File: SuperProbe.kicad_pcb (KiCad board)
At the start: 2 copper layers, 100 x 45 mm, 66 parts, among them J1 Conn_01x01, J10 Conn_01x01, J11 Conn_01x01, J12 Conn_01x01, J13 Conn_01x01, J14 Conn_01x01, J15 Conn_01x01, J16 Conn_01x01, J17 Conn_01x02, J2 Conn_01x01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

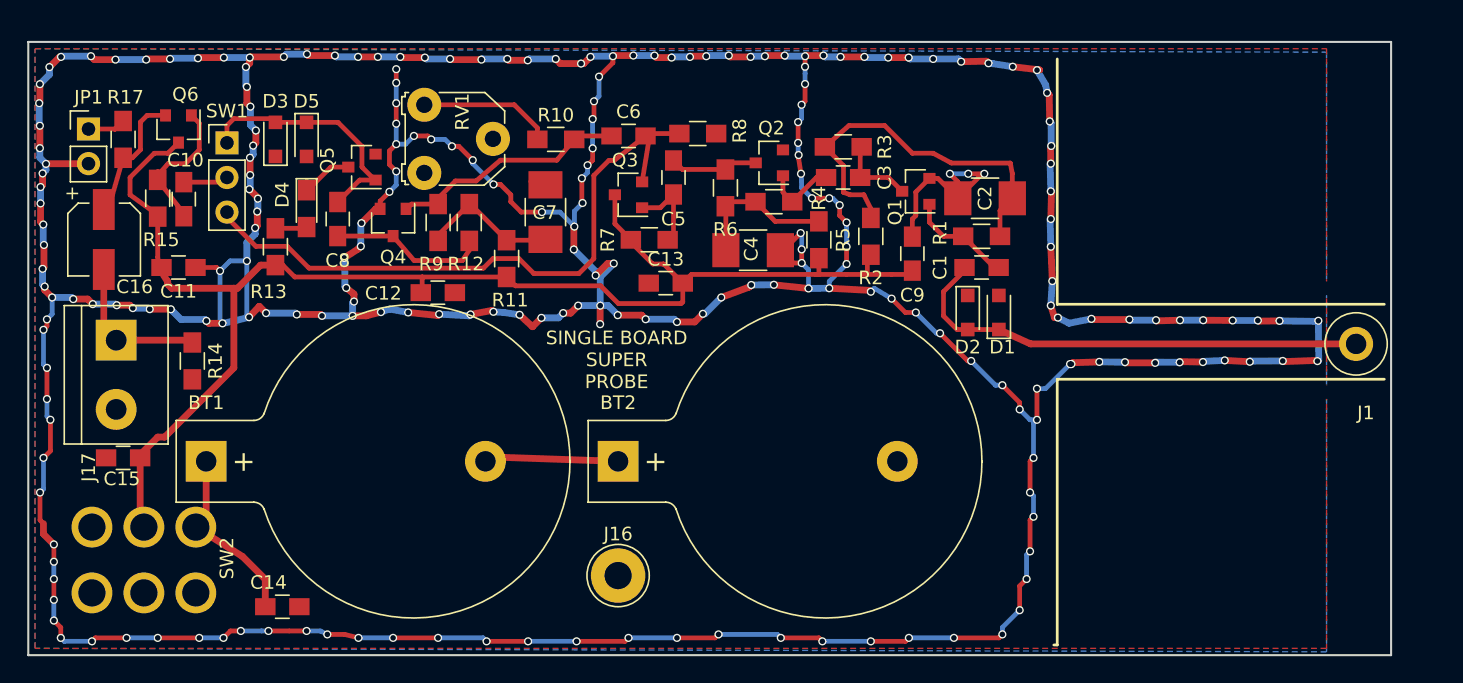
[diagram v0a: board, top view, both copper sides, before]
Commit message: Uses 9 volt battery and board shrink
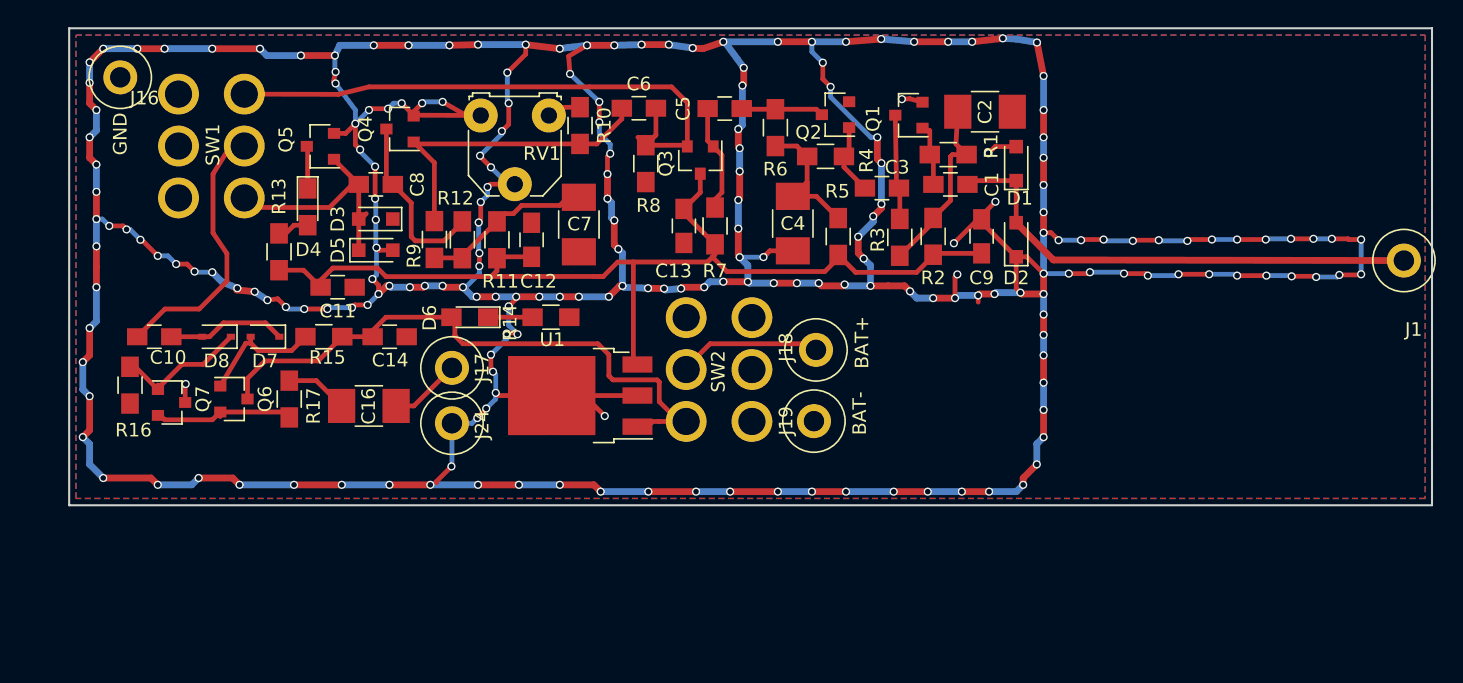
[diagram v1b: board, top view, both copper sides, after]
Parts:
- removed BT1, BT2: Battery_Cell, Battery_Holders:Keystone_103_1x20mm-CoinCell
- removed C15: 100 nF, Capacitors_SMD:C_0805_HandSoldering
- removed JP1: Jumper_NO_Small, Pin_Headers:Pin_Header_Straight_1x02_Pitch2.54mm
- added D6: LED, LEDs:LED_0805_HandSoldering, F.Cu at (70.4, 102.2)
- added D7: 1N4148WS, Diodes_SMD:D_SOD-323, F.Cu at (55.4, 103.6)
- added D8: 1N4148WS, Diodes_SMD:D_SOD-323, F.Cu at (51.8, 103.6)
- added J18: Conn_01x01, Connectors:1pin, F.Cu at (95.8, 104.6)
- added J19: Conn_01x01, Connectors:1pin, F.Cu at (95.7, 109.8)
- added J20: Conn_01x01, SuperProbe:BigSlot, F.Cu at (108.2, 110.0)
- added J21: Conn_01x01, SuperProbe:BigSlot, F.Cu at (102.0, 110.0)
- added J22: Conn_01x01, SuperProbe:BigSlot, F.Cu at (108.2, 84.3)
- added J23: Conn_01x01, SuperProbe:BigSlot, F.Cu at (102.1, 84.4)
- added J24: Conn_01x01, Connectors:1pin, F.Cu at (69.1, 110.0)
- added Q7: MMBT3906, TO_SOT_Packages_SMD:SOT-23, F.Cu at (48.5, 108.5)
- added R16: 10k, Resistors_SMD:R_0805_HandSoldering, F.Cu at (45.5, 107.2)
- added U1: LM78M05_TO252, TO_SOT_Packages_SMD:TO-252-3_TabPin2, F.Cu at (78.5, 108.0)
- C14: value 100 nF -> 1 uF
- C16: value 100 uF -> 22 uF; footprint Capacitors_SMD:CP_Elec_5x5.3 -> Capacitors_SMD:C_1210_HandSoldering
- J17: value Conn_01x02 -> Conn_01x01; footprint Connectors_Terminal_Blocks:TerminalBlock_bornier-2_P5.08mm -> Connectors:1pin
- R14: value 10k -> 1k
- R15: value 3M3 -> 10k
- R17: value 10k -> 100R
- SW1: footprint Pin_Headers:Pin_Header_Straight_1x03_Pitch2.54mm -> SuperProbe:DPDTsmallswitch
- moved J16 51.7 mm to (44.8, 84.6)
- moved SW2 41.5 mm to (91.1, 109.8), turned to 90 degrees
- moved J15 39.9 mm to (114.6, 82.8)
- moved J14 29.7 mm to (114.6, 87.1)
- moved J8 28.2 mm to (114.6, 113.8)
- moved R14 26.5 mm to (76.3, 102.2), turned to 0 degrees
- moved J17 24.7 mm to (69.1, 105.9), turned to 0 degrees
- moved C16 23.0 mm to (63.0, 108.7), turned to 180 degrees
- moved R17 22.6 mm to (57.1, 108.2), turned to 270 degrees
- moved C14 21.3 mm to (64.5, 103.6)
- moved Q6 20.2 mm to (53.1, 108.2), turned to 0 degrees
- moved J9 17.8 mm to (114.6, 93.0)
- moved J7 17.8 mm to (114.6, 109.2)
- moved R15 15.9 mm to (59.7, 103.6), turned to 180 degrees
- moved J13 13.4 mm to (136.9, 94.5)
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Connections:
- C14 pad 2: Net-(BT1-Pad1) -> +9V
- J17 pad 1: Net-(C16-Pad2) -> Net-(C16-Pad1)
- Q6 pad 1: Net-(C10-Pad1) -> Net-(D7-Pad2)
- Q6 pad 2: Net-(C16-Pad1) -> Net-(Q6-Pad2)
- Q6 pad 3: +5V -> +9V
- R14 pad 1: Net-(C16-Pad2) -> Net-(D6-Pad1)
- R15 pad 1: +5V -> +9V
- R15 pad 2: Net-(C10-Pad1) -> Net-(D7-Pad2)
- R17 pad 1: Net-(C16-Pad1) -> Net-(C16-Pad2)
- R17 pad 2: Net-(JP1-Pad1) -> Net-(Q6-Pad2)
- SW2 pad 1: Net-(BT1-Pad1) -> (no net)
- SW2 pad 2: +5V -> (no net)
- SW2 pad 4: (no net) -> +9V
- SW2 pad 5: (no net) -> Net-(J18-Pad1)
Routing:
- net +9V: track 0.00 -> 46.2 mm
- net +5V: track 108.0 -> 76.1 mm
- net GND: track 490.7 -> 514.7 mm, vias 233 -> 216
- net Net-(C10-Pad2): track 3.31 -> 21.6 mm
- net Net-(BT1-Pad1): track 15.3 -> 0.00 mm
- net Net-(C2-Pad1): track 28.2 -> 13.5 mm
- net Net-(Q6-Pad2): track 0.00 -> 10.6 mm
- net Net-(J18-Pad1): track 0.00 -> 10.6 mm
- net Net-(D8-Pad1): track 0.00 -> 10.1 mm
- net Net-(BT1-Pad2): track 9.88 -> 0.00 mm
- net Net-(C16-Pad2): track 14.3 -> 4.61 mm
- net Net-(D7-Pad2): track 0.00 -> 9.16 mm
- net Net-(R10-Pad2): track 10.1 -> 2.53 mm
- net Net-(C6-Pad1): track 17.7 -> 23.3 mm
- net Net-(C16-Pad1): track 9.79 -> 5.25 mm
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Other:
- board size 100 x 45 mm -> 100 x 35 mm
- board text added: "BAT+"
- board text added: "BAT-"
- board text added: "GND"

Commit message: Cleaned up the board slightly
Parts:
- C10: value 10 nF -> 100 nF
- C16, C2, C4, C7: footprint Capacitors_SMD:C_1210_HandSoldering -> Capacitors_SMD:C_0805_HandSoldering
- C8: value 360 pF -> 330 pF
- J1, J16, J17, J18, J19, J24: footprint Connectors:1pin -> SuperProbe:PadHole
- Q6: value MMBT3904 -> S8050
- Q7: value MMBT3906 -> S8550
- R1, R4, R7, R9: value 3M3 -> 2M2
- R17: value 100R -> 47R
- moved J8 1.01 mm to (114.5, 112.8)
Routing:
- net GND: track 514.7 -> 512.7 mm
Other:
- board size 100 x 35 mm -> 100 x 34 mm
- board text added: "SPK+"
- board text added: "SPK-"

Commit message: Eliminated unneeded diode
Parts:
- removed D3: LRB751V, Diodes_SMD:D_SOD-323_HandSoldering
- Q6: value S8050 -> SS8050
- Q7: value S8550 -> SS8550
- moved D5 2.29 mm to (63.5, 95.0)
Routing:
- net Net-(C8-Pad1): track 17.6 -> 14.6 mm
- net GND: track 512.7 -> 513.0 mm, vias 216 -> 215
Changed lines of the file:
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@@
 (kicad_pcb (version 4) (host pcbnew 4.0.7)
   (general
-    (links 95)
+    (links 93)
     (no_connects 0)
     (area 40.002381 78.05638 143.68562 117.528699)
     (thickness 1.6)
     (drawings 10)
-    (tracks 822)
+    (tracks 819)
     (zones 0)
-    (modules 75)
+    (modules 74)
     (nets 29)
   )
@@
     )
   )
-  (module Diodes_SMD:D_SOD-323_HandSoldering (layer F.Cu)
-    (at 63.5 94.996 180)
-    (descr SOD-323)
-    (tags SOD-323)
-    (attr smd)
-    (fp_text reference D3 (at 2.794 0 270) (layer F.SilkS)
-      (effects (font (size 1 1) (thickness 0.15)))
-    )
-    (fp_text value LRB751V (at 0.1 1.9 180) (layer F.Fab)
-      (effects (font (size 1 1) (thickness 0.15)))
-    )
-    (fp_text user %R (at 0 -1.85 180) (layer F.Fab)
-      (effects (font (size 1 1) (thickness 0.15)))
-    )
-    (fp_line (start -1.9 -0.85) (end -1.9 0.85) (layer F.SilkS) (width 0.12))
-    (fp_line (start 0.2 0) (end 0.45 0) (layer F.Fab) (width 0.1))
-    (fp_line (start 0.2 0.35) (end -0.3 0) (layer F.Fab) (width 0.1))
-    (fp_line (start 0.2 -0.35) (end 0.2 0.35) (layer F.Fab) (width 0.1))
-    (fp_line (start -0.3 0) (end 0.2 -0.35) (layer F.Fab) (width 0.1))
-    (fp_line (start -0.3 0) (end -0.5 0) (layer F.Fab) (width 0.1))
-    (fp_line (start -0.3 -0.35) (end -0.3 0.35) (layer F.Fab) (width 0.1))
-    (fp_line (start -0.9 0.7) (end -0.9 -0.7) (layer F.Fab) (width 0.1))
-    (fp_line (start 0.9 0.7) (end -0.9 0.7) (layer F.Fab) (width 0.1))
-    (fp_line (start 0.9 -0.7) (end 0.9 0.7) (layer F.Fab) (width 0.1))
-    (fp_line (start -0.9 -0.7) (end 0.9 -0.7) (layer F.Fab) (width 0.1))
-    (fp_line (start -2 -0.95) (end 2 -0.95) (layer F.CrtYd) (width 0.05))
-    (fp_line (start 2 -0.95) (end 2 0.95) (layer F.CrtYd) (width 0.05))
-    (fp_line (start -2 0.95) (end 2 0.95) (layer F.CrtYd) (width 0.05))
-    (fp_line (start -2 -0.95) (end -2 0.95) (layer F.CrtYd) (width 0.05))
-    (fp_line (start -1.9 0.85) (end 1.25 0.85) (layer F.SilkS) (width 0.12))
-    (fp_line (start -1.9 -0.85) (end 1.25 -0.85) (layer F.SilkS) (width 0.12))
-    (pad 1 smd rect (at -1.25 0 180) (size 1 1) (layers F.Cu F.Paste F.Mask)
-      (net 1 GND))
-    (pad 2 smd rect (at 1.25 0 180) (size 1 1) (layers F.Cu F.Paste F.Mask)
-      (net 13 "Net-(C8-Pad1)"))
-    (model ${KISYS3DMOD}/Diodes_SMD.3dshapes/D_SOD-323.wrl
-      (at (xyz 0 0 0))
-      (scale (xyz 1 1 1))
-      (rotate (xyz 0 0 0))
-    )
-  )
   (module LEDs:LED_0805_HandSoldering (layer F.Cu)
     (at 58.5 94.1 270)
@@
   )
   (module Diodes_SMD:D_SOD-323_HandSoldering (layer F.Cu)
-    (at 63.5 97.282)
+    (at 63.5 94.996)
     (descr SOD-323)
     (tags SOD-323)
@@
       (effects (font (size 1 1) (thickness 0.15)))
     )
-    (fp_text value S8050 (at 0 2.032) (layer F.Fab)
+    (fp_text value SS8050 (at 0 2.032) (layer F.Fab)
       (effects (font (size 1 1) (thickness 0.15)))
     )
@@
       (effects (font (size 1 1) (thickness 0.15)))
     )
-    (fp_text value S8550 (at 0 2.5) (layer F.Fab)
+    (fp_text value SS8550 (at 0 2.5) (layer F.Fab)
       (effects (font (size 1 1) (thickness 0.15)))
     )
@@
     (effects (font (size 1 1) (thickness 0.15)) (justify mirror))
   )
+  (segment (start 64.75 94.996) (end 63.754 94.996) (width 0.35) (layer F.Cu) (net 1))
+  (via (at 63.5 95.05) (size 0.6) (drill 0.4) (layers F.Cu B.Cu) (net 1))
+  (segment (start 63.754 94.996) (end 63.5 94.742) (width 0.35) (layer F.Cu) (net 1))
   (segment (start 68 112.5) (end 68 111.07) (width 0.35) (layer B.Cu) (net 1))
   (segment (start 68 111.07) (end 69.088 109.982) (width 0.35) (layer B.Cu) (net 1))
@@
   (via (at 66.11 104.87) (size 0.6) (drill 0.4) (layers F.Cu B.Cu) (net 1))
   (segment (start 65.766 104.526) (end 66.11 104.87) (width 0.35) (layer F.Cu) (net 1))
-  (segment (start 63.55 97.1) (end 64.568 97.1) (width 0.35) (layer F.Cu) (net 1))
-  (via (at 63.55 97.1) (size 0.6) (drill 0.4) (layers F.Cu B.Cu) (net 1))
-  (segment (start 64.568 97.1) (end 64.75 97.282) (width 0.35) (layer F.Cu) (net 1))
+  (segment (start 64.568 94.814) (end 64.75 94.996) (width 0.35) (layer F.Cu) (net 1) (status 30))
   (segment (start 72.3 107.75) (end 72.3 106.4) (width 0.35) (layer B.Cu) (net 1))
   (segment (start 72.3 106.4) (end 72.1 106.2) (width 0.35) (layer B.Cu) (net 1))
@@
   (segment (start 63.55 97.1) (end 63.5 97.05) (width 0.35) (layer B.Cu) (net 1))
   (segment (start 63.5 97.05) (end 63.5 95.05) (width 0.35) (layer B.Cu) (net 1))
-  (via (at 63.5 95.05) (size 0.6) (drill 0.4) (layers F.Cu B.Cu) (net 1))
   (segment (start 60.436 88.712) (end 61.288 88.712) (width 0.35) (layer F.Cu) (net 1))
   (segment (start 61.288 88.712) (end 62 88) (width 0.35) (layer F.Cu) (net 1))
@@
   (segment (start 69.85 97.71) (end 72.39 95.17) (width 0.35) (layer F.Cu) (net 12))
   (segment (start 72.39 95.17) (end 72.724 95.17) (width 0.35) (layer F.Cu) (net 12))
+  (segment (start 62.25 94.996) (end 62.25 92.456) (width 0.35) (layer F.Cu) (net 13))
   (segment (start 62.25 92.456) (end 61.794 92.456) (width 0.35) (layer F.Cu) (net 13))
   (segment (start 61.794 92.456) (end 60.1 94.15) (width 0.35) (layer F.Cu) (net 13))
   (segment (start 60.1 94.15) (end 54.55 94.15) (width 0.35) (layer F.Cu) (net 13))
   (segment (start 54.55 94.15) (end 53.85 93.45) (width 0.35) (layer F.Cu) (net 13))
-  (segment (start 62.25 94.996) (end 62.196 94.996) (width 0.35) (layer F.Cu) (net 13))
   (segment (start 53.934 93.366) (end 53.85 93.45) (width 0.35) (layer F.Cu) (net 13) (status 30))
   (segment (start 60.436 90.612) (end 60.436 90.642) (width 0.35) (layer F.Cu) (net 13))
   (segment (start 60.436 90.642) (end 62.25 92.456) (width 0.35) (layer F.Cu) (net 13))
-  (segment (start 62.25 92.456) (end 62.25 94.996) (width 0.35) (layer F.Cu) (net 13))
-  (segment (start 62.25 97.282) (end 62.25 95.15) (width 0.35) (layer F.Cu) (net 13))
-  (segment (start 62.25 95.15) (end 62.8 94.6) (width 0.35) (layer F.Cu) (net 13))
   (segment (start 64.278 88.392) (end 64.278 91.984) (width 0.35) (layer F.Cu) (net 14))
   (segment (start 64.278 91.984) (end 64.75 92.456) (width 0.35) (layer F.Cu) (net 14))
